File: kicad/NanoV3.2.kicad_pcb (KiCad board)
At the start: 2 copper layers, 43.2 x 17.8 mm, 23 parts, among them IC2 LM1117, IC3 ATMEGA328P-AU, P1 TTL, P2 OUT, P3 INPUT, Q1 BC237, Y1 16MHz

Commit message: finished layout
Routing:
- net /D11/MOSI: track 26.9 -> 23.8 mm, vias 3 -> 1

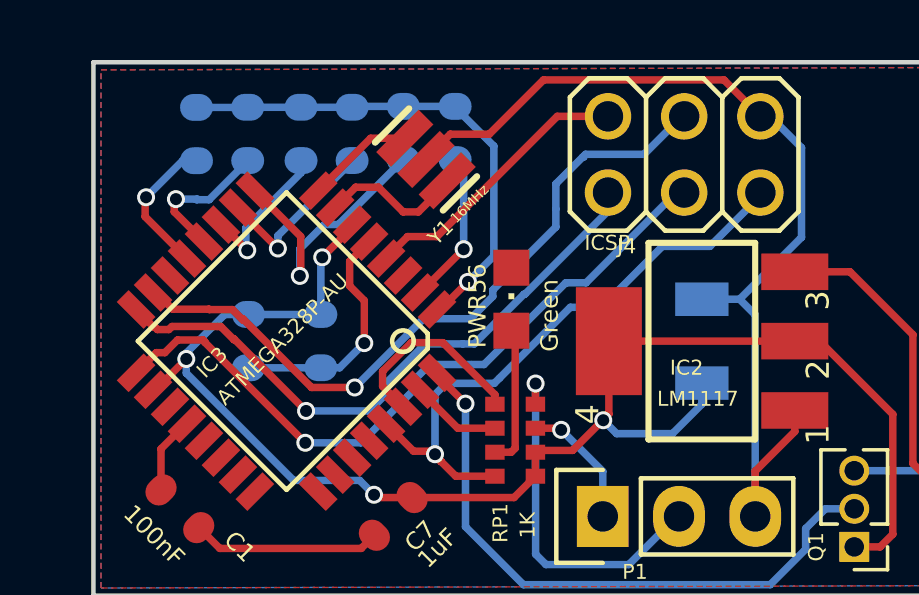
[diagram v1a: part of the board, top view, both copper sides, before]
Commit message: updated jumpper pad
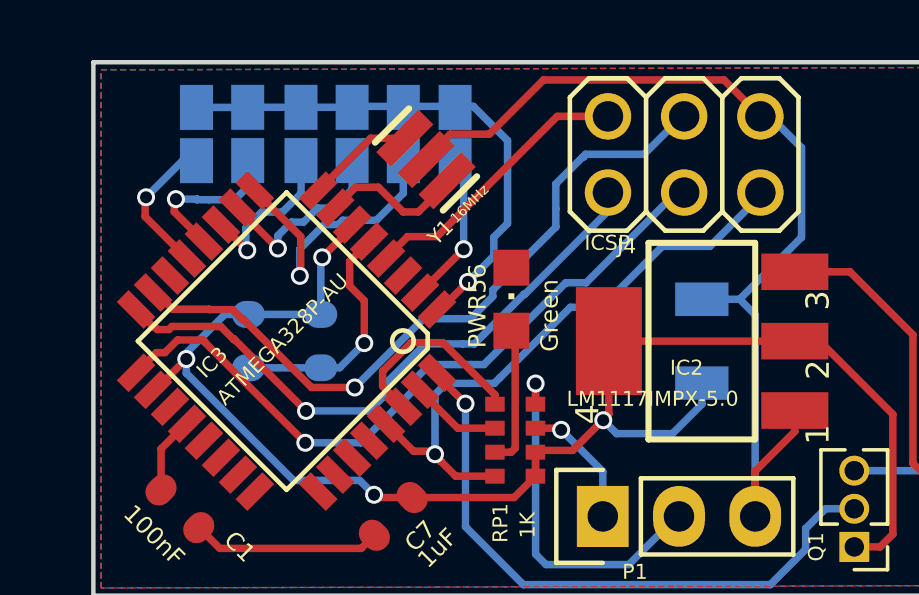
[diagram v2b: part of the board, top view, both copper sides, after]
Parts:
- IC2: value LM1117 -> LM1117IMPX-5.0
- JP1, JP2, JP3, JP4, JP5, JP6: footprint C0603-ROUND -> autoSwitch:SMD-Jummper
- RL1: value ~ -> relay
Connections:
- IC3 pad 14: (no net) -> /D10
- IC3 pad 19: (no net) -> /A6
- IC3 pad 22: (no net) -> /A7
- IC3 pad 23: (no net) -> /A0
- IC3 pad 24: (no net) -> /A1
- IC3 pad 25: (no net) -> /A2
- IC3 pad 26: (no net) -> /A3
- IC3 pad 27: (no net) -> /A4
- IC3 pad 28: (no net) -> /A5
- RL1 pad 10: (no net) -> Net-(RL1-Pad10)
- RL1 pad 14: (no net) -> Net-(RL1-Pad14)
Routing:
- net /D7: track 5.00 -> 5.81 mm
- net /D3: track 16.9 -> 17.7 mm
- net /D5: track 9.54 -> 10.2 mm
- net /D6: track 5.87 -> 6.44 mm
- net /D8: track 5.24 -> 5.76 mm

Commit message: Version V0.9
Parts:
- IC2: value LM1117IMPX-5.0 -> LM1117
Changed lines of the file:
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@@
       (effects (font (size 0.5 0.5) (thickness 0.061772)) (justify right top))
     )
-    (fp_text value LM1117IMPX-5.0 (at -1.63068 1.22428 180) (layer F.SilkS)
+    (fp_text value LM1117 (at -1.63068 1.22428 180) (layer F.SilkS)
       (effects (font (size 0.5 0.5) (thickness 0.061772)) (justify right top))
     )
@@
     (tags CAPACITOR)
     (attr smd)
-    (fp_text reference JP1 (at -3.4544 0.06604 90) (layer B.SilkS)
-      (effects (font (size 1.27 1.27) (thickness 0.1016)) (justify mirror))
+    (fp_text reference JP1 (at -2.99212 0.02032 90) (layer B.SilkS)
+      (effects (font (size 0.7 0.7) (thickness 0.1016)) (justify mirror))
     )
     (fp_text value ~ (at 2.921 -1.397 90) (layer B.SilkS)
@@
     (tags CAPACITOR)
     (attr smd)
-    (fp_text reference JP2 (at -3.4544 0.07112 90) (layer B.SilkS)
-      (effects (font (size 1.27 1.27) (thickness 0.1016)) (justify mirror))
+    (fp_text reference JP2 (at -2.95148 0.02032 90) (layer B.SilkS)
+      (effects (font (size 0.7 0.7) (thickness 0.1016)) (justify mirror))
     )
     (fp_text value ~ (at 2.921 -1.397 90) (layer B.SilkS)
@@
     (tags CAPACITOR)
     (attr smd)
-    (fp_text reference JP3 (at -3.43916 0.07112 90) (layer B.SilkS)
-      (effects (font (size 1.27 1.27) (thickness 0.1016)) (justify mirror))
+    (fp_text reference JP3 (at -2.9972 0.04064 90) (layer B.SilkS)
+      (effects (font (size 0.7 0.7) (thickness 0.1016)) (justify mirror))
     )
     (fp_text value ~ (at 2.921 -1.397 90) (layer B.SilkS)
@@
     (tags CAPACITOR)
     (attr smd)
-    (fp_text reference JP4 (at -3.42392 0.06604 90) (layer B.SilkS)
-      (effects (font (size 1.27 1.27) (thickness 0.1016)) (justify mirror))
+    (fp_text reference JP4 (at -2.91592 -0.0254 90) (layer B.SilkS)
+      (effects (font (size 0.7 0.7) (thickness 0.1016)) (justify mirror))
     )
     (fp_text value ~ (at 2.921 -1.397 90) (layer B.SilkS)
@@
     (tags CAPACITOR)
     (attr smd)
-    (fp_text reference JP5 (at -3.42392 0.0762 90) (layer B.SilkS)
-      (effects (font (size 1.27 1.27) (thickness 0.1016)) (justify mirror))
+    (fp_text reference JP5 (at -2.83464 -0.01524 90) (layer B.SilkS)
+      (effects (font (size 0.7 0.7) (thickness 0.1016)) (justify mirror))
     )
     (fp_text value ~ (at 2.921 -1.397 90) (layer B.SilkS)
@@
     (tags CAPACITOR)
     (attr smd)
-    (fp_text reference JP6 (at -3.46456 0.0762 90) (layer B.SilkS)
-      (effects (font (size 1.27 1.27) (thickness 0.1016)) (justify mirror))
+    (fp_text reference JP6 (at -2.8702 0.06604 90) (layer B.SilkS)
+      (effects (font (size 0.7 0.7) (thickness 0.1016)) (justify mirror))
     )
     (fp_text value ~ (at 2.921 -1.397 90) (layer B.SilkS)

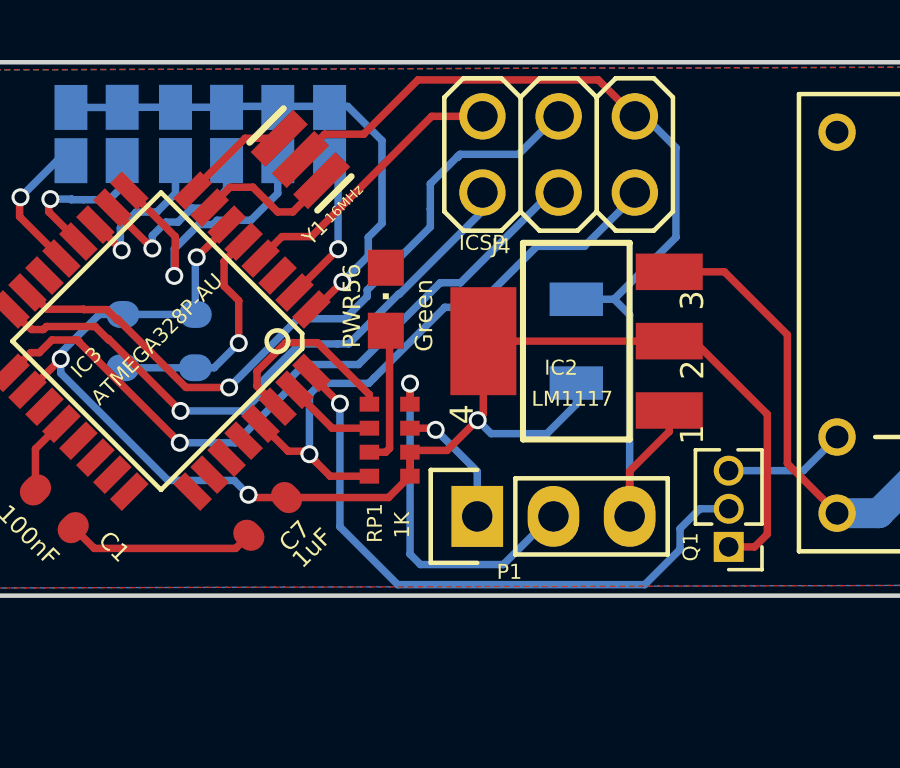
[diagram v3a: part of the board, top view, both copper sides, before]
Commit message: updated RP1 network and crytal footprint
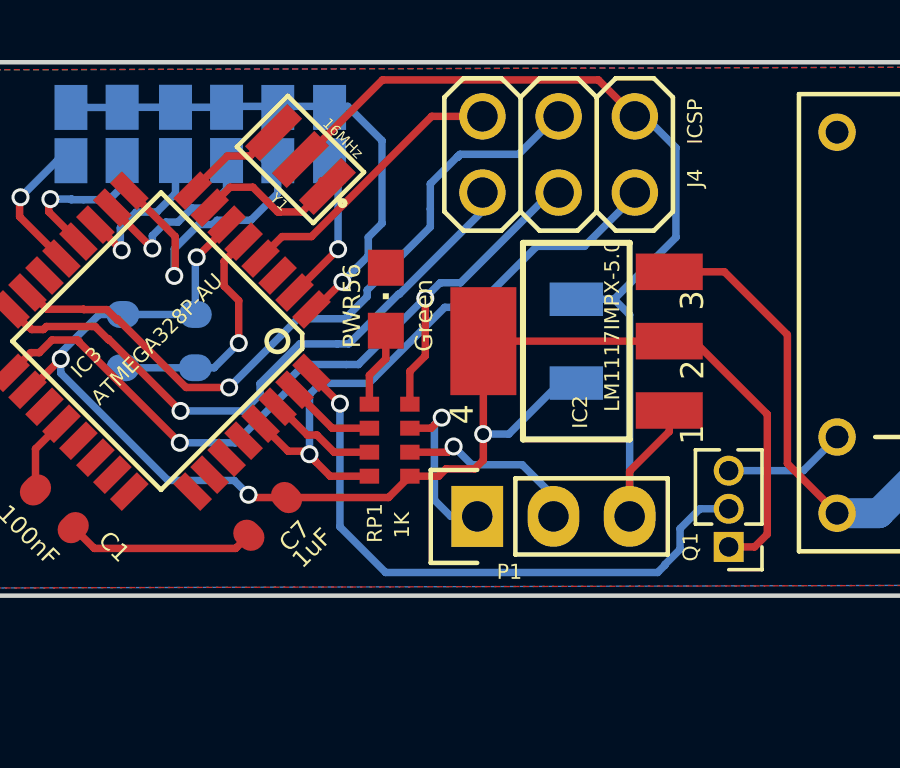
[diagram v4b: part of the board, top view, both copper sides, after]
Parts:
- IC2: value LM1117 -> LM1117IMPX-5.0
- RL1: value relay -> ~
- Y1: footprint RESONATOR -> autoSwitch:Crystal3215
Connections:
- IC3 pad 14: /D10 -> (no net)
- IC3 pad 19: /A6 -> (no net)
- IC3 pad 22: /A7 -> (no net)
- IC3 pad 23: /A0 -> (no net)
- IC3 pad 24: /A1 -> (no net)
- IC3 pad 25: /A2 -> (no net)
- IC3 pad 26: /A3 -> (no net)
- IC3 pad 27: /A4 -> (no net)
- IC3 pad 28: /A5 -> (no net)
- RL1 pad 10: Net-(RL1-Pad10) -> (no net)
- RL1 pad 14: Net-(RL1-Pad14) -> (no net)
- RP1 pad 1: /D0/RX -> /N$3
- RP1 pad 3: /N$3 -> /D0/RX
- RP1 pad 6: +5V -> Net-(P1-Pad2)
- RP1 pad 8: Net-(P1-Pad2) -> /D13/SCK
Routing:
- net Net-(P1-Pad2): track 12.0 -> 6.38 mm
- net /D13/SCK: track 24.0 -> 27.8 mm, vias 1 -> 2
- net /D0/RX: track 6.64 -> 3.69 mm
- net /N$3: track 4.70 -> 2.86 mm
- net /TX: track 4.34 -> 5.71 mm

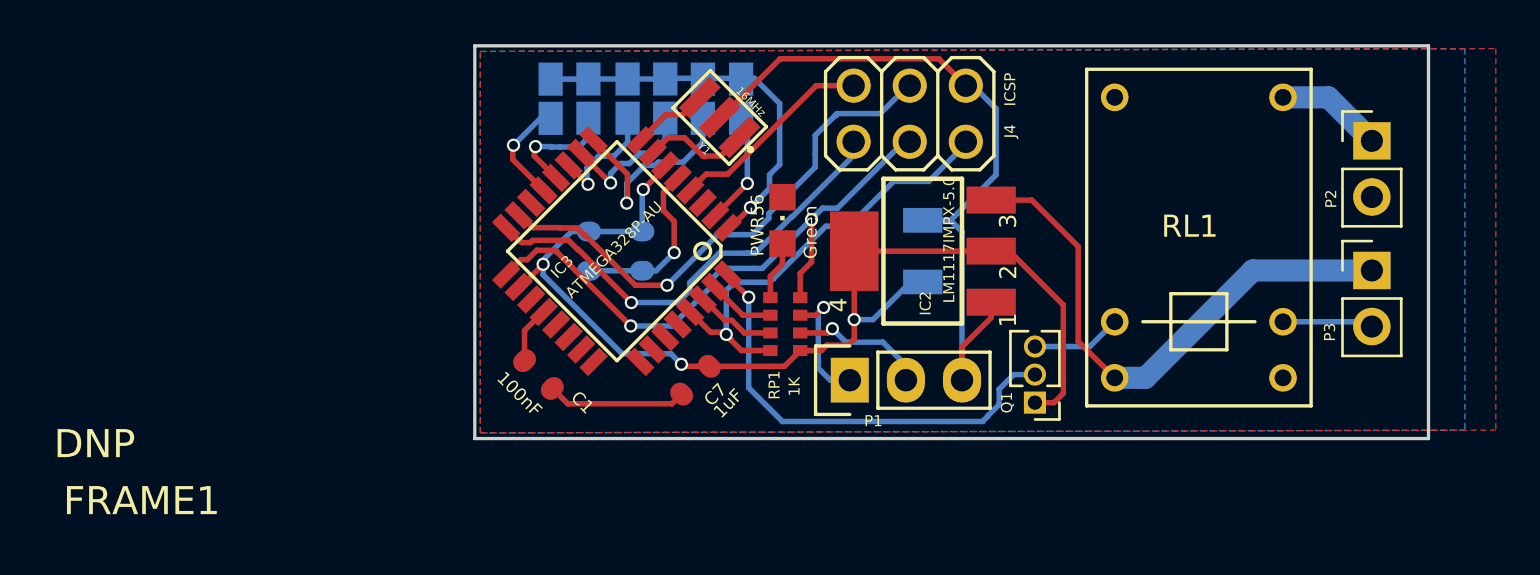
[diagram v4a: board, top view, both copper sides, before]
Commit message: updated Q1 footprint and updated routing
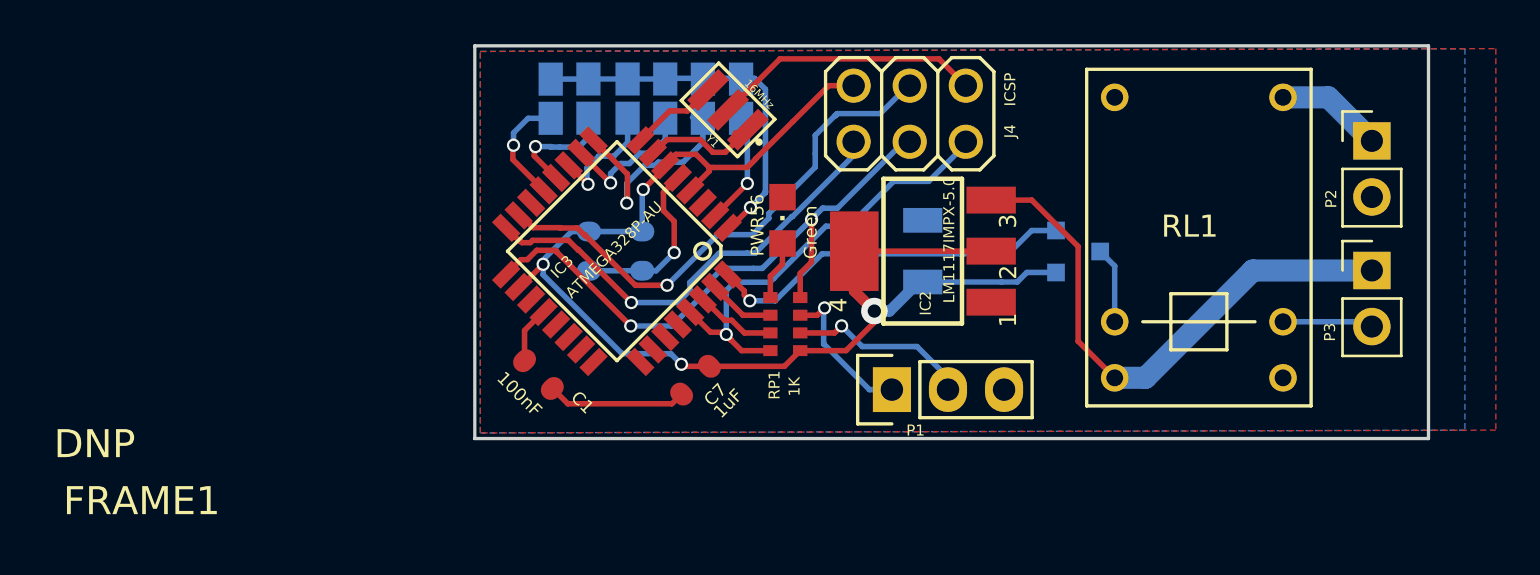
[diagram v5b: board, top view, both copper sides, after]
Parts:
- Q1: value BC237 -> s9014; footprint Pin_Headers:Pin_Header_Straight_1x03_Pitch1.27mm -> TO_SOT_Packages_SMD:SOT-23; moved to B.Cu
- moved Q1 7.12 mm to (154.2, 105.4), turned to 90 degrees
- moved P1 1.95 mm to (145.8, 111.7)
- moved Y1 0.51 mm to (138.4, 99.0)
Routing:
- net COM: track 52.1 -> 31.9 mm
- net /D2: track 20.4 -> 17.0 mm
- net Net-(P1-Pad2): track 6.38 -> 8.42 mm
- net /TX: track 5.71 -> 7.59 mm
- net /D9: track 4.82 -> 5.61 mm
- net +5V: track 60.1 -> 60.7 mm
- net Net-(Q1-Pad3): track 4.08 -> 3.45 mm
- net /N$1: track 3.50 -> 4.02 mm
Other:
- net class w0.5: via_drill 0.8 -> 0.6

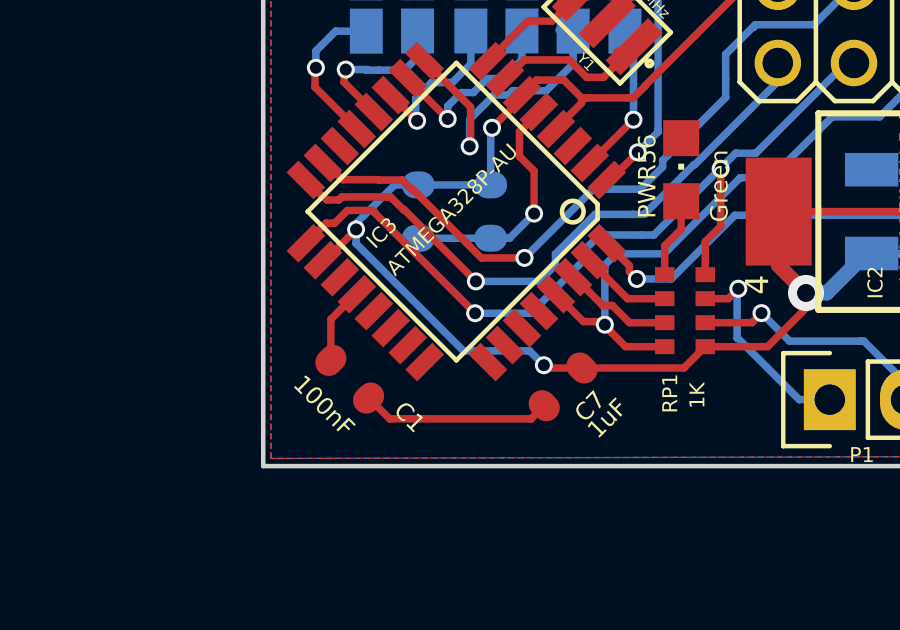
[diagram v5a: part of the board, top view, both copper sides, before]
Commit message: minor update of routing
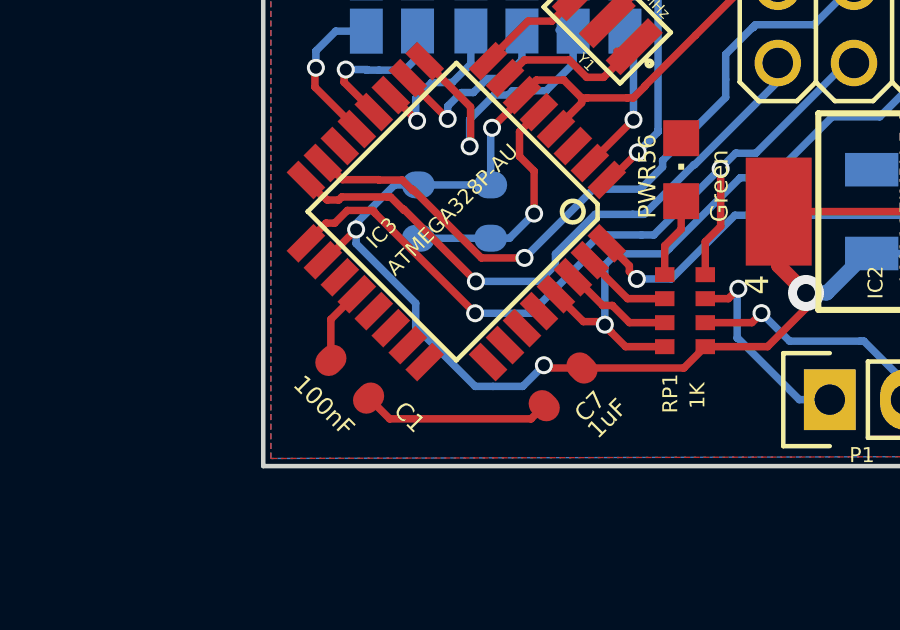
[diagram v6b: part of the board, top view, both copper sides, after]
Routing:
- net +5V: track 60.7 -> 61.8 mm
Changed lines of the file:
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@@
     (thickness 1.6)
     (drawings 89)
-    (tracks 319)
+    (tracks 322)
     (zones 0)
     (modules 23)
@@
   (segment (start 163.50488 108.60532) (end 167.3098 108.60532) (width 0.25) (layer Bottom) (net 1))
   (segment (start 167.3098 108.60532) (end 167.52824 108.82376) (width 0.25) (layer Bottom) (net 1))
+  (segment (start 131.99364 108.46308) (end 131.99364 109.25556) (width 0.25) (layer Bottom) (net 2))
+  (segment (start 133.97484 111.23676) (end 134.5692 111.23676) (width 0.25) (layer Bottom) (net 2))
+  (segment (start 131.99364 109.25556) (end 133.97484 111.23676) (width 0.25) (layer Bottom) (net 2))
+  (segment (start 135.5598 111.23676) (end 136.26592 110.53064) (width 0.25) (layer Bottom) (net 2))
+  (segment (start 136.26592 110.53064) (end 136.358662 110.623382) (width 0.25) (layer Top) (net 2))
+  (via (at 136.26592 110.53064) (size 0.6) (drill 0.4) (layers Top Bottom) (net 2))
+  (segment (start 136.358662 110.623382) (end 137.534618 110.623382) (width 0.25) (layer Top) (net 2))
+  (segment (start 134.5692 111.23676) (end 135.5598 111.23676) (width 0.25) (layer Bottom) (net 2))
   (segment (start 141.645 109.912) (end 143.72224 109.912) (width 0.25) (layer Top) (net 2))
   (segment (start 145.00352 108.63072) (end 145.00352 108.12272) (width 0.25) (layer Top) (net 2))
@@
   (segment (start 147.193 106.807) (end 146.64436 106.807) (width 0.25) (layer Bottom) (net 2))
   (segment (start 130.00736 106.00436) (end 130.00736 106.4768) (width 0.25) (layer Bottom) (net 2))
-  (segment (start 135.7884 110.05312) (end 136.26592 110.53064) (width 0.25) (layer Bottom) (net 2))
-  (segment (start 133.58368 110.05312) (end 135.7884 110.05312) (width 0.25) (layer Bottom) (net 2))
-  (segment (start 130.00736 106.4768) (end 133.58368 110.05312) (width 0.25) (layer Bottom) (net 2))
+  (segment (start 130.00736 106.4768) (end 131.99364 108.46308) (width 0.25) (layer Bottom) (net 2))
   (segment (start 136.668169 102.657516) (end 136.668169 102.640471) (width 0.25) (layer Top) (net 2))
-  (segment (start 136.358662 110.623382) (end 137.534618 110.623382) (width 0.25) (layer Top) (net 2))
-  (via (at 136.26592 110.53064) (size 0.6) (drill 0.4) (layers Top Bottom) (net 2))
-  (segment (start 136.26592 110.53064) (end 136.358662 110.623382) (width 0.25) (layer Top) (net 2))
   (segment (start 134.493 104.521) (end 134.493 102.66172) (width 0.25) (layer Bottom) (net 2))
   (segment (start 134.53872 102.616) (end 135.536798 101.617922) (width 0.25) (layer Top) (net 2))
